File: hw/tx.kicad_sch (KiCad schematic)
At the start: 27 parts, among them Q301 IRLML2060, Q302 IRLML2060, Q303 IRLML2060, Q304 IRLML2060, T301 BN-43-202_DualPri_CTSec, U301 UCC27523DGN, U302 UCC27523DGN

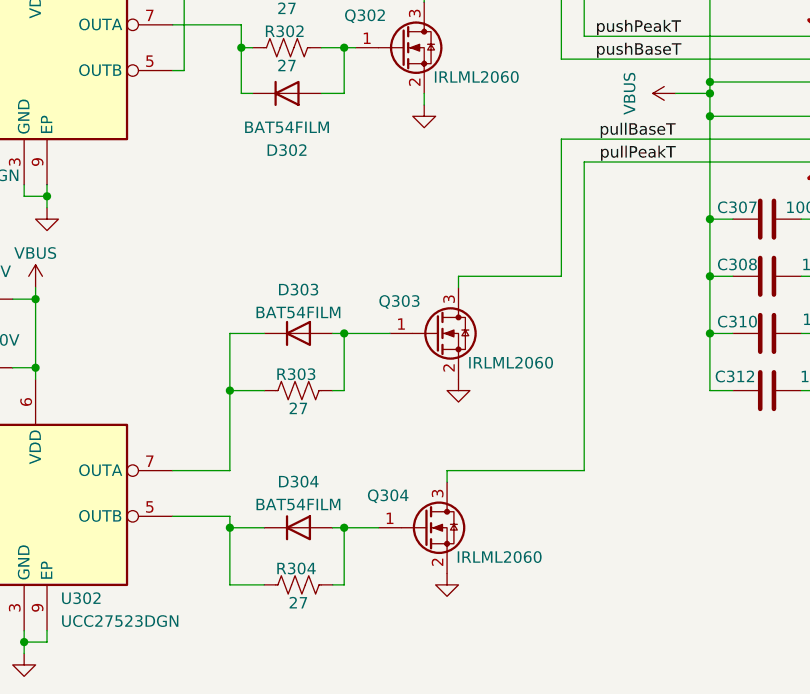
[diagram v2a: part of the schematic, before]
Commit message: Various schematic clean ups. Improved/fixed decoupling around relays. Filter Vdd for TCXO and SI5351 to try to minimize modulation of the clock freq by noise
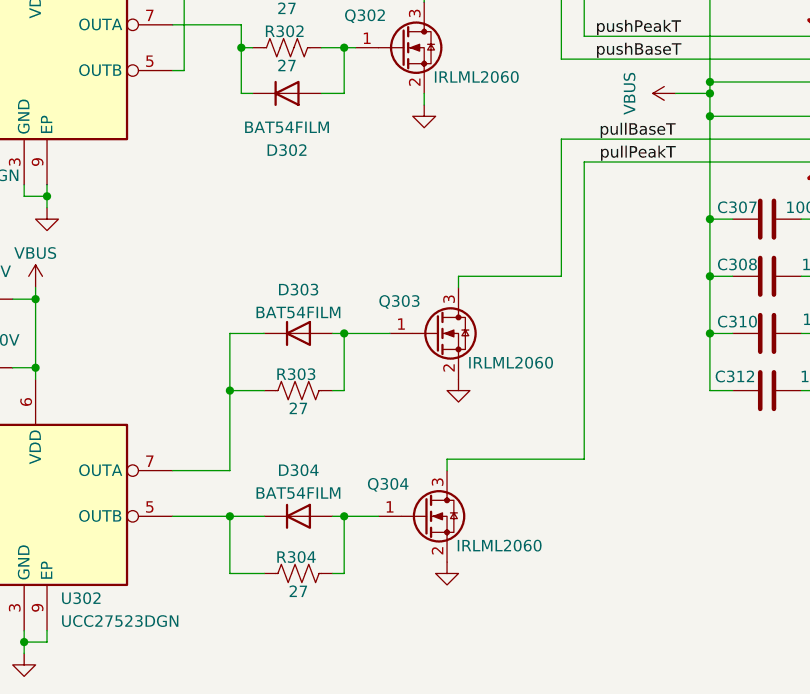
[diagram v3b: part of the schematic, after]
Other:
- moved on the sheet: D304, Q304, R304
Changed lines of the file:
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@@
 	)
 	(junction
-		(at 165.1 114.3)
+		(at 165.1 113.03)
 		(diameter 0)
 		(color 0 0 0 0)
@@
 	)
 	(junction
-		(at 152.4 114.3)
+		(at 152.4 113.03)
 		(diameter 0)
 		(color 0 0 0 0)
@@
 	(wire
 		(pts
-			(xy 152.4 113.03) (xy 152.4 114.3)
-		)
-		(stroke
-			(width 0)
-			(type default)
-		)
-	)
-	(wire
-		(pts
 			(xy 229.87 86.36) (xy 229.87 92.71)
 		)
@@
 	(wire
 		(pts
-			(xy 152.4 114.3) (xy 156.21 114.3)
+			(xy 152.4 113.03) (xy 156.21 113.03)
 		)
 		(stroke
@@
 	(wire
 		(pts
-			(xy 152.4 114.3) (xy 152.4 120.65)
+			(xy 152.4 113.03) (xy 152.4 119.38)
 		)
 		(stroke
@@
 	(wire
 		(pts
-			(xy 152.4 120.65) (xy 156.21 120.65)
-		)
-		(stroke
-			(width 0)
-			(type default)
-		)
-	)
-	(wire
-		(pts
-			(xy 176.53 107.95) (xy 176.53 109.22)
+			(xy 152.4 119.38) (xy 156.21 119.38)
 		)
 		(stroke
@@
 	(wire
 		(pts
-			(xy 165.1 114.3) (xy 168.91 114.3)
+			(xy 165.1 113.03) (xy 168.91 113.03)
 		)
 		(stroke
@@
 	(wire
 		(pts
-			(xy 165.1 114.3) (xy 165.1 120.65)
+			(xy 165.1 113.03) (xy 165.1 119.38)
 		)
 		(stroke
@@
 	(wire
 		(pts
-			(xy 146.05 113.03) (xy 152.4 113.03)
+			(xy 176.53 106.68) (xy 176.53 107.95)
 		)
 		(stroke
@@
 	(wire
 		(pts
-			(xy 163.83 114.3) (xy 165.1 114.3)
+			(xy 163.83 113.03) (xy 165.1 113.03)
 		)
 		(stroke
@@
 	(wire
 		(pts
-			(xy 176.53 107.95) (xy 191.77 107.95)
+			(xy 176.53 106.68) (xy 191.77 106.68)
 		)
 		(stroke
@@
 	(wire
 		(pts
-			(xy 163.83 120.65) (xy 165.1 120.65)
+			(xy 163.83 119.38) (xy 165.1 119.38)
 		)
 		(stroke
@@
 	(wire
 		(pts
-			(xy 191.77 73.66) (xy 191.77 107.95)
+			(xy 191.77 73.66) (xy 191.77 106.68)
 		)
 		(stroke
@@
 	(wire
 		(pts
+			(xy 146.05 113.03) (xy 152.4 113.03)
+		)
+		(stroke
+			(width 0)
+			(type default)
+		)
+	)
+	(wire
+		(pts
 			(xy 217.17 62.23) (xy 189.23 62.23)
 		)
@@
 	(symbol
 		(lib_id "Transistor_FET:BS170F")
-		(at 173.99 114.3 0)
+		(at 173.99 113.03 0)
 		(unit 1)
 		(exclude_from_sim no)
@@
 		(dnp no)
 		(property "Reference" "Q304"
-			(at 167.64 110.744 0)
+			(at 167.64 109.474 0)
 			(effects
 				(font
@@
 		)
 		(property "Value" "IRLML2060"
-			(at 177.546 117.602 0)
+			(at 177.546 116.332 0)
 			(effects
 				(font
@@
 		)
 		(property "Footprint" "Package_TO_SOT_SMD:SOT-23"
-			(at 179.07 116.205 0)
+			(at 179.07 114.935 0)
 			(effects
 				(font
@@
 		)
 		(property "Datasheet" ""
-			(at 179.07 118.11 0)
+			(at 179.07 116.84 0)
 			(effects
 				(font
@@
 		)
 		(property "Description" "MOSFETs MOSFT 60V 1.2A 480mOhm 0.7nC Qg"
-			(at 173.99 114.3 0)
+			(at 173.99 113.03 0)
 			(effects
 				(font
@@
 		)
 		(property "LCSC" ""
-			(at 173.99 114.3 0)
+			(at 173.99 113.03 0)
 			(effects
 				(font
@@
 		)
 		(property "MFG" "Infineon"
-			(at 173.99 114.3 0)
+			(at 173.99 113.03 0)
 			(effects
 				(font
@@
 		)
 		(property "MPN" "IRLML2060TRPBF"
-			(at 173.99 114.3 0)
+			(at 173.99 113.03 0)
 			(effects
 				(font
@@
 		)
 		(property "Mouser_PN" "942-IRLML2060TRPBF"
-			(at 173.99 114.3 0)
+			(at 173.99 113.03 0)
 			(effects
 				(font
@@
 		)
 		(property "Field10" ""
-			(at 173.99 114.3 0)
+			(at 173.99 113.03 0)
 			(effects
 				(font
@@
 		)
 		(property "MouserPN" ""
-			(at 173.99 114.3 0)
+			(at 173.99 113.03 0)
 			(effects
 				(font
@@
 	(symbol
 		(lib_id "Diode:1N4148W")
-		(at 160.02 114.3 0)
+		(at 160.02 113.03 0)
 		(unit 1)
 		(exclude_from_sim no)
@@
 		(dnp no)
 		(property "Reference" "D304"
-			(at 160.02 109.22 0)
+			(at 160.02 107.95 0)
 			(effects
 				(font
@@
 		)
 		(property "Value" "BAT54FILM"
-			(at 160.02 111.76 0)
+			(at 160.02 110.49 0)
 			(effects
 				(font
@@
 		)
 		(property "Footprint" "Diode_SMD:D_SOD-123"
-			(at 160.02 118.745 0)
+			(at 160.02 117.475 0)
 			(effects
 				(font
@@
 		)
 		(property "Datasheet" "https://www.vishay.com/docs/85748/1n4148w.pdf"
-			(at 160.02 114.3 0)
+			(at 160.02 113.03 0)
 			(effects
 				(font
@@
 		)
 		(property "Description" "75V 0.15A Fast Switching Diode, SOD-123"
-			(at 160.02 114.3 0)
+			(at 160.02 113.03 0)
 			(effects
 				(font
@@
 		)
 		(property "Sim.Device" "D"
-			(at 160.02 114.3 0)
+			(at 160.02 113.03 0)
 			(effects
 				(font
@@
 		)
 		(property "Sim.Pins" "1=K 2=A"
-			(at 160.02 114.3 0)
+			(at 160.02 113.03 0)
 			(effects
 				(font
@@
 		)
 		(property "Field10" ""
-			(at 160.02 114.3 0)
+			(at 160.02 113.03 0)
 			(effects
 				(font
@@
 		)
 		(property "MFG" "ST"
-			(at 160.02 114.3 0)
+			(at 160.02 113.03 0)
 			(effects
 				(font
@@
 		)
 		(property "MPN" "BAT54ZFILM"
-			(at 160.02 114.3 0)
+			(at 160.02 113.03 0)
 			(effects
 				(font
@@
 		)
 		(property "Mouser_PN" "511-BAT54FILM"
-			(at 160.02 114.3 0)
+			(at 160.02 113.03 0)
 			(effects
 				(font
@@
 		)
 		(property "MouserPN" ""
-			(at 160.02 114.3 0)
+			(at 160.02 113.03 0)
 			(effects
 				(font
@@
 		)
 		(property "LCSC" ""
-			(at 160.02 114.3 0)
+			(at 160.02 113.03 0)
 			(effects
 				(font
@@
 	(symbol
 		(lib_id "Device:R_US")
-		(at 160.02 120.65 90)
+		(at 160.02 119.38 90)
 		(unit 1)
 		(exclude_from_sim no)
@@
 		(dnp no)
 		(property "Reference" "R304"
-			(at 159.766 118.872 90)
+			(at 159.766 117.602 90)
 			(effects
 				(font
@@
 		)
 		(property "Value" "27"
-			(at 160.02 122.682 90)
+			(at 160.02 121.412 90)
 			(effects
 				(font
@@
 		)
 		(property "Footprint" "Resistor_SMD:R_0402_1005Metric"
-			(at 160.274 119.634 90)
+			(at 160.274 118.364 90)
 			(effects
 				(font
@@
 		)
 		(property "Datasheet" "~"
-			(at 160.02 120.65 0)
+			(at 160.02 119.38 0)
 			(effects
 				(font
@@
 		)
 		(property "Description" "Resistor, US symbol"
-			(at 160.02 120.65 0)
+			(at 160.02 119.38 0)
 			(effects
 				(font
@@
 		)
 		(property "LCSC" ""
-			(at 160.02 120.65 90)
+			(at 160.02 119.38 90)
 			(effects
 				(font
@@
 		)
 		(property "MFG" ""
-			(at 160.02 120.65 90)
+			(at 160.02 119.38 90)
 			(effects
 				(font
@@
 		)
 		(property "MPN" ""
-			(at 160.02 120.65 90)
+			(at 160.02 119.38 90)
 			(effects
 				(font
@@
 		)
 		(property "Mouser_PN" ""
-			(at 160.02 120.65 90)
+			(at 160.02 119.38 90)
 			(effects
 				(font
@@
 		)
 		(property "Field10" ""
-			(at 160.02 120.65 90)
+			(at 160.02 119.38 90)
 			(effects
 				(font
@@
 		)
 		(property "MouserPN" ""
-			(at 160.02 120.65 90)
+			(at 160.02 119.38 90)
 			(effects
 				(font
@@
 	(symbol
 		(lib_id "power:GND")
-		(at 176.53 119.38 0)
+		(at 176.53 118.11 0)
 		(unit 1)
 		(exclude_from_sim no)
@@
 		(fields_autoplaced yes)
 		(property "Reference" "#PWR0313"
-			(at 176.53 125.73 0)
+			(at 176.53 124.46 0)
 			(effects
 				(font
@@
 		)
 		(property "Value" "GND"
-			(at 176.53 124.46 0)
+			(at 176.53 123.19 0)
 			(effects
 				(font
@@
 		)
 		(property "Footprint" ""
-			(at 176.53 119.38 0)
+			(at 176.53 118.11 0)
 			(effects
 				(font
@@
 		)
 		(property "Datasheet" ""
-			(at 176.53 119.38 0)
+			(at 176.53 118.11 0)
 			(effects
 				(font
@@
 		)
 		(property "Description" "Power symbol creates a global label with name \"GND\" , ground"
-			(at 176.53 119.38 0)
+			(at 176.53 118.11 0)
 			(effects
 				(font

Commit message: Simplify. Put exciter stuff onto transmitter sheet.
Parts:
- added C301, C302, C303, C304, C311, C312, C322, C323, C324, C325, C326, C328: 100nF X7R 50V, Capacitor_SMD:C_0402_1005Metric, symbol Device:C
- added C319, C320, C321, C327: 1uF X5R 25V, Capacitor_SMD:C_0402_1005Metric, symbol Device:C
- added FB301: 600@1A, Inductor_SMD:L_0603_1608Metric, symbol Device:FerriteBead_Small
- added R305, R306: 27, Resistor_SMD:R_0402_1005Metric, symbol Device:R_US
- added R307, R308: 5.1k, Resistor_SMD:R_0402_1005Metric, symbol Device:R_US
- added TP301: A, TestPoint:TestPoint_Pad_1.5x1.5mm, symbol Connector:TestPoint
- added TP302: B, TestPoint:TestPoint_Pad_1.5x1.5mm, symbol Connector:TestPoint
- added U301: LCMXO2-256HC-4SG32C, Package_DFN_QFN:QFN-32-1EP_5x5mm_P0.5mm_EP3.1x3.1mm_ThermalVias, symbol Library:LCMXO2-SG32
- added U304: SI5351A-B-GT, Package_SO:MSOP-10_3x3mm_P0.5mm, symbol Oscillator:Si5351A-B-GT
- added Y301: 20MHz, Library:ECSTXO201633400TR, symbol Library:ECS-TX-5032-200
- renumbered C301 to C305, C302 to C306, C303 to C307, C304 to C308, C305 to C309, C306 to C310, C307 to C313, C308 to C314, C309 to C315, C310 to C316, C311 to C317, C312 to C318, U301 to U302, U302 to U303
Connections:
- net GND: now also C301.1, C302.1, C303.1, C304.1, C311.1, C312.1, C319.2, C320.2, C321.2, C322.1, C323.1, C324.1, C326.1, C327.2, C328.2, U301.22 (GND), U301.3 (GND), U301.33 (THERM), U304.8 (GND), Y301.2 (GND)
- net nPullBase: now also U301.12 (PCLKC2_0)
- net nPullPeak: now also U301.11 (PCLKT2_0)
- net nPushBase: now also U301.14 (PCLKC2_1)
- net nPushPeak: now also U301.13 (PCLKT2_1)
- new net: R305.1, U301.21 (PCLKT1_0)
- new net: TP302.1, U301.28 (SCL/PCLKT0_0)
- new net: TP301.1, U301.27 (SDA/PCLKC0_0)
- new net: C325.1, Y301.3 (OUTPUT)
- new net: R306.2, U304.9 (CLK1)
- new net: C325.2, U304.2 (XA)
- new net: R305.2, U304.10 (CLK0)
- new net +3.3V: C301.2, C302.2, C303.2, C304.2, C311.2, C312.2, C322.2, C326.2, FB301.1, R307.2, R308.2, U301.15 (VCCIO2), U301.18 (VCC), U301.19 (VCCIO1), U301.2 (VCC), U301.24 (VCCIO0), U301.31 (VCCIO0), U301.6 (VCCIO3), U301.7 (VCCIO2)
- new net +VDDA: C319.1, C320.1, C321.1, C323.2, C324.2, C327.1, C328.1, FB301.2, U304.1 (VDD), U304.7 (VDDO), Y301.4 (VDD)
- new net cpldDONE: U301.23 (DONE)
- new net cpldMISO: U301.10 (SO/SPISO)
- new net cpldMOSI: U301.17 (SI/SISPI)
- new net cpldNCS: U301.8 (CSSPIN)
- new net cpldPROG: U301.25 (PROG)
- new net cpldSCK: U301.9 (MCLK/CCLK)
- new net txSCL: R307.1, U304.4 (SCL)
- new net txSDA: R308.1, U304.5 (SDA)
- new net txco: R306.1
- no-connect marks 0 -> 11

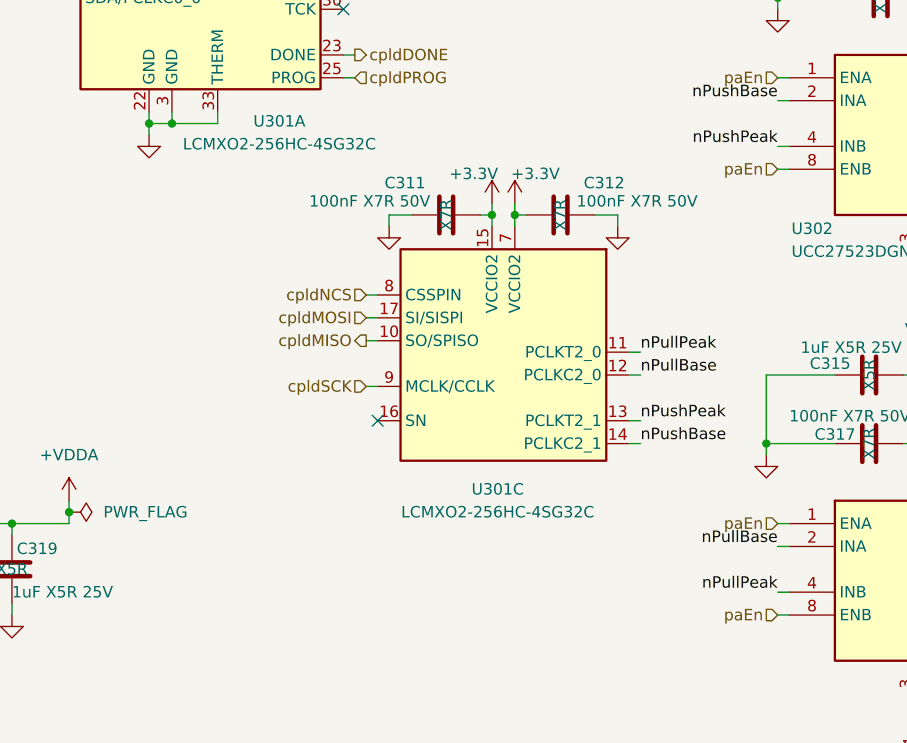
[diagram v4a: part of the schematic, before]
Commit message: Add stitched GND zone around edge of PCB on all layers and pretty up the mounting holes with vias as well.
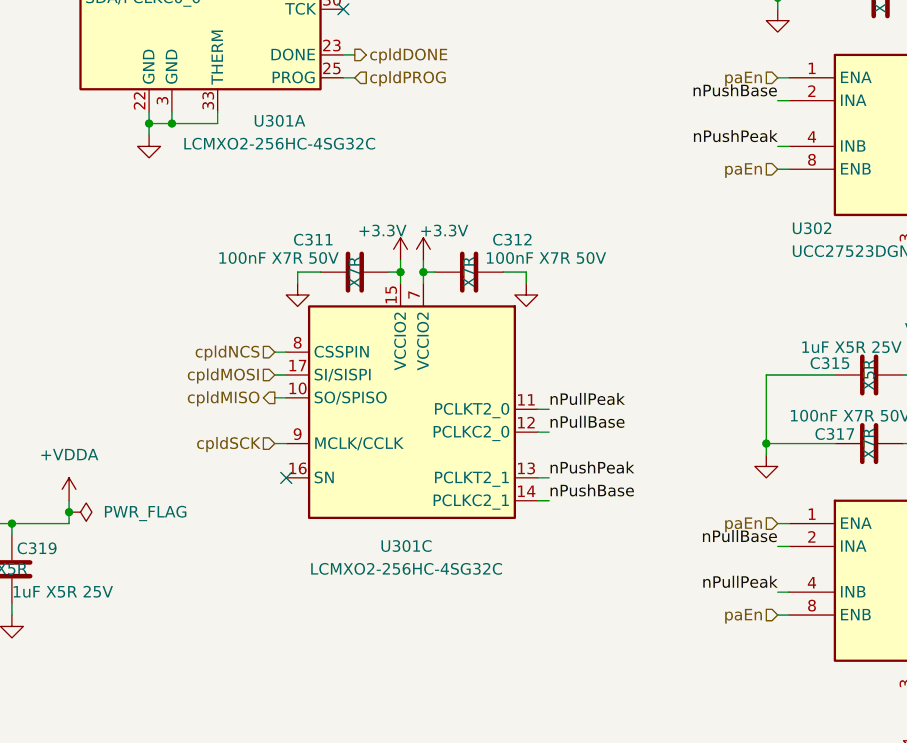
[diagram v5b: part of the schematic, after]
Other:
- moved on the sheet: C311, C312, U301C
